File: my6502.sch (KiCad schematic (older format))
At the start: 64 parts, among them SW1 SW_MEC_5G, SW2 SW_MEC_5G, SW3 SW_Push_DPDT, SW4 SW_Push, SW5 SW_Push, SW6 SW_Push, SW7 SW_Push, SW8 SW_Push, SW9 SW_Push, U1 74HC00, U10 74HC00, U11 74HC00, U12 74HC00, U13 74HC00, U14 74HC00, U15 74HC00, U16 74HC00, U17 74HC00, U18 LM555xN, U2 LM555xN, U3 W65C02S, U4 LM555xN, U5 28C256, U6 65C22, U7 CY62256-70PC, U8 HD44780, U9 74HC00, X1 CXO_DIP14

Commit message: placed most components
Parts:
- removed U10, U11, U13, U14, U15, U16: 74HC00, Package_DIP:DIP-14_W7.62mm_LongPads, symbol 74xx:74HC00
- added C16, C17, C18: 100n, Capacitor_THT:C_Disc_D5.1mm_W3.2mm_P5.00mm, symbol Device:C
- added J1, J2, J3: Conn_01x08, Connector_PinHeader_2.54mm:PinHeader_1x08_P2.54mm_Vertical, symbol Connector_Generic:Conn_01x08
- added unit 2 of U12
- added unit 3 of U12
- added unit 4 of U12
- added unit 5 of U12
- added unit 2 of U17
- added unit 3 of U17
- added unit 4 of U17
- added unit 5 of U17
- added unit 2 of U9
- added unit 3 of U9
- added unit 4 of U9
- added unit 5 of U9
- D1, D2, D3: footprint LED_THT:LED_D5.0mm -> LED_THT:LED_D3.0mm
- JP1: footprint (none) -> Connector_PinHeader_2.54mm:PinHeader_1x03_P2.54mm_Vertical
- JP2, JP3, JP4: footprint (none) -> Connector_PinHeader_2.54mm:PinHeader_1x02_P2.54mm_Vertical
- SW1: value SW_MEC_5G -> Switch; footprint (none) -> Button_Switch_THT:SW_PUSH_6mm; symbol Switch:SW_MEC_5G -> Switch:SW_Push
- SW2: footprint (none) -> Button_Switch_THT:SW_PUSH_6mm; symbol Switch:SW_MEC_5G -> Switch:SW_Push
- SW4: footprint (none) -> Button_Switch_THT:SW_PUSH_6mm; PartID (none) -> Adafruit 4183
- SW5, SW6, SW7, SW8, SW9: footprint (none) -> Button_Switch_THT:SW_PUSH_6mm
- U8: footprint (none) -> Display:WC1602A
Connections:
- net +5V: now also C16.1, C17.1, C18.1, U12.14 (VCC), U9.14 (VCC)
- net A0: now also J1.1 (Pin_1)
- net A1: now also J1.2 (Pin_2)
- net A10: now also J3.3 (Pin_3)
- net A11: now also J3.4 (Pin_4)
- net A12: now also U1.13, J3.5 (Pin_5); no longer U1.2
- net A13: now also J3.6 (Pin_6)
- net A14: now also J3.7 (Pin_7)
- net A15: now also U1.1, U1.2, J3.8 (Pin_8); no longer U1.12, U1.13
- net A2: now also J1.3 (Pin_3)
- net A3: now also J1.4 (Pin_4)
- net A4: now also J1.5 (Pin_5)
- net A5: now also J1.6 (Pin_6)
- net A6: now also J1.7 (Pin_7)
- net A7: now also J1.8 (Pin_8)
- net A8: now also J3.1 (Pin_1)
- net A9: now also J3.2 (Pin_2)
- net CLK: now also U12.8
- net CLKSEL: now also U9.4, U9.5
- net D0: now also J2.1 (Pin_1)
- net D1: now also J2.2 (Pin_2)
- net D2: now also J2.3 (Pin_3)
- net D3: now also J2.4 (Pin_4)
- net D4: now also J2.5 (Pin_5)
- net D5: now also J2.6 (Pin_6)
- net D6: now also J2.7 (Pin_7)
- net D7: now also J2.8 (Pin_8)
- net GND: now also SW2.2, C16.2, C17.2, C18.2, U12.12, U12.13, U12.7 (GND), U17.10, U17.12, U17.13, U17.4, U17.5, U17.9, U9.7 (GND); no longer SW1.2 (A), SW2.3 (B), SW2.4 (B)
- net MCLK: now also U9.10
- net RESET: no longer SW2.2 (A)
- net ~A15: now also U1.3; no longer U1.11
- net at R3.2, U4.2 (TR): now also SW1.2; no longer SW1.3 (B), SW1.4 (B)
- net at U1.8: now also U1.12; no longer U1.1
- net at U17.2, U6.23 (CS2B): now also U1.11; no longer U1.3
- net at U9.3: now also U9.12
- net at JP1.1 (A): now also U9.11
- net at JP1.2 (C): now also U12.4
- net at U12.3: now also U12.5
- new net: U9.6, U9.9
- new net: U9.13, U9.8
- new net: U12.10, U12.6, U12.9
- no-connect marks 13 -> 16

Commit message: USB connector, overvoltage protection, ...
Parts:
- added D4: D_Zener, Diode_THT:D_A-405_P7.62mm_Horizontal, symbol Device:D_Zener
- added D5: LED, LED_THT:LED_D3.0mm, symbol Device:LED
- added J4: USB_B_Micro, Connector_USB:USB_Micro-B_Molex_47346-0001, symbol Connector:USB_B_Micro
- added R12: ? (low res), Resistor_THT:R_Axial_DIN0207_L6.3mm_D2.5mm_P7.62mm_Horizontal, symbol Device:R
- added R13: 220, Resistor_THT:R_Axial_DIN0207_L6.3mm_D2.5mm_P7.62mm_Horizontal, symbol Device:R
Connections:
- net +5V: now also D4.1 (K), D5.2 (A), R12.1
- net GND: now also D4.2 (A), J4.5 (GND), R13.1
- new net: D5.1 (K), R13.2
- new net USBVCC: J4.1 (VBUS), R12.2
- no-connect marks 16 -> 21
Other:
- note added: "TODO:\n- Mounting holes\n- Check if any more 6502 pins\n should be accessible (RDY? NMI?)\n- Validate all components! Not the least the USB conn.\n- Place all decoupler caps close to their IC's\n- Fancy silkscreen!\n- Is HLT connected anywhere?"
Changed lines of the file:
@@
 Text Label 12050 5600 0    50   ~ 0
 D7
-Wire Bus Line
-	9200 800  9200 2150
-Wire Bus Line
-	6900 800  6900 2150
-Wire Bus Line
-	7300 800  7300 2850
-Wire Bus Line
-	4900 800  4900 2850
-Wire Bus Line
-	14000 900  14000 2550
-Wire Bus Line
-	9650 900  9650 3550
-Wire Bus Line
-	4200 800  4200 4950
-Wire Bus Line
-	11700 800  11700 5500
 $Comp
 L Connector_Generic:Conn_01x08 J1
@@
 	1    0    0    -1
 $EndComp
+$Comp
+L Connector:USB_B_Micro J4
+U 1 1 60B35F2D
+P 10150 6900
+F 0 "J4" H 10207 7367 50  0000 C CNN
+F 1 "USB_B_Micro" H 10207 7276 50  0000 C CNN
+F 2 "Connector_USB:USB_Micro-B_Molex_47346-0001" H 10300 6850 50  0001 C CNN
+F 3 "~" H 10300 6850 50  0001 C CNN
+	1    10150 6900
+	1    0    0    -1
+$EndComp
+$Comp
+L power:GND #PWR0163
+U 1 1 60B392C5
+P 10150 7400
+F 0 "#PWR0163" H 10150 7150 50  0001 C CNN
+F 1 "GND" H 10155 7227 50  0000 C CNN
+F 2 "" H 10150 7400 50  0001 C CNN
+F 3 "" H 10150 7400 50  0001 C CNN
+	1    10150 7400
+	1    0    0    -1
+$EndComp
+Wire Wire Line
+	10150 7300 10150 7400
+Wire Wire Line
+	10450 6700 10800 6700
+Text Label 10500 6700 0    50   ~ 0
+USBVCC
+$Comp
+L Device:R R12
+U 1 1 60BB1CFB
+P 10950 6700
+F 0 "R12" H 11020 6746 50  0000 L CNN
+F 1 "? (low res)" H 11020 6655 50  0000 L CNN
+F 2 "Resistor_THT:R_Axial_DIN0207_L6.3mm_D2.5mm_P7.62mm_Horizontal" V 10880 6700 50  0001 C CNN
+F 3 "~" H 10950 6700 50  0001 C CNN
+	1    10950 6700
+	0    1    -1   0
+$EndComp
+$Comp
+L Device:D_Zener D4
+U 1 1 60BBC9CB
+P 11200 6950
+F 0 "D4" V 11154 7030 50  0000 L CNN
+F 1 "D_Zener" V 11245 7030 50  0000 L CNN
+F 2 "Diode_THT:D_A-405_P7.62mm_Horizontal" H 11200 6950 50  0001 C CNN
+F 3 "~" H 11200 6950 50  0001 C CNN
+	1    11200 6950
+	0    1    1    0
+$EndComp
+Wire Wire Line
+	11100 6700 11200 6700
+Wire Wire Line
+	11200 6700 11200 6800
+$Comp
+L power:GND #PWR0164
+U 1 1 60C904E5
+P 11200 7200
+F 0 "#PWR0164" H 11200 6950 50  0001 C CNN
+F 1 "GND" H 11205 7027 50  0000 C CNN
+F 2 "" H 11200 7200 50  0001 C CNN
+F 3 "" H 11200 7200 50  0001 C CNN
+	1    11200 7200
+	1    0    0    -1
+$EndComp
+Wire Wire Line
+	11200 7100 11200 7200
+$Comp
+L power:+5V #PWR0165
+U 1 1 60CCD1B2
+P 11200 6600
+F 0 "#PWR0165" H 11200 6450 50  0001 C CNN
+F 1 "+5V" H 11215 6773 50  0000 C CNN
+F 2 "" H 11200 6600 50  0001 C CNN
+F 3 "" H 11200 6600 50  0001 C CNN
+	1    11200 6600
+	-1   0    0    -1
+$EndComp
+Wire Wire Line
+	11200 6600 11200 6700
+Connection ~ 11200 6700
+NoConn ~ 10450 6900
+NoConn ~ 10450 7000
+NoConn ~ 10450 7100
+NoConn ~ 10050 7300
+NoConn ~ 12450 6250
+$Comp
+L Device:R R13
+U 1 1 60E322F4
+P 11700 7000
+F 0 "R13" H 11770 7046 50  0000 L CNN
+F 1 "220" H 11770 6955 50  0000 L CNN
+F 2 "Resistor_THT:R_Axial_DIN0207_L6.3mm_D2.5mm_P7.62mm_Horizontal" V 11630 7000 50  0001 C CNN
+F 3 "~" H 11700 7000 50  0001 C CNN
+	1    11700 7000
+	1    0    0    1
+$EndComp
+$Comp
+L Device:LED D5
+U 1 1 60E5E64D
+P 11500 6700
+F 0 "D5" H 11650 6650 50  0000 C CNN
+F 1 "LED" H 11500 6800 50  0000 C CNN
+F 2 "LED_THT:LED_D3.0mm" H 11500 6700 50  0001 C CNN
+F 3 "~" H 11500 6700 50  0001 C CNN
+	1    11500 6700
+	-1   0    0    1
+$EndComp
+Wire Wire Line
+	11200 6700 11350 6700
+Wire Wire Line
+	11650 6700 11700 6700
+Wire Wire Line
+	11700 6700 11700 6850
+$Comp
+L power:GND #PWR0166
+U 1 1 60F053B9
+P 11700 7200
+F 0 "#PWR0166" H 11700 6950 50  0001 C CNN
+F 1 "GND" H 11705 7027 50  0000 C CNN
+F 2 "" H 11700 7200 50  0001 C CNN
+F 3 "" H 11700 7200 50  0001 C CNN
+	1    11700 7200
+	1    0    0    -1
+$EndComp
+Wire Wire Line
+	11700 7150 11700 7200
+Wire Bus Line
+	9200 800  9200 2150
+Wire Bus Line
+	6900 800  6900 2150
+Wire Bus Line
+	7300 800  7300 2850
+Wire Bus Line
+	4900 800  4900 2850
+Wire Bus Line
+	14000 900  14000 2550
+Wire Bus Line
+	9650 900  9650 3550
+Wire Bus Line
+	4200 800  4200 4950
+Wire Bus Line
+	11700 800  11700 5500
+Text Notes -2500 600  0    50   ~ 0
+TODO:\n- Mounting holes\n- Check if any more 6502 pins\n    should be accessible (RDY? NMI?)\n- Validate all components! Not the least the USB conn.\n- Place all decoupler caps close to their IC's\n- Fancy silkscreen!\n- Is HLT connected anywhere?
 $EndSCHEMATC

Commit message: Mostly minor adjustments
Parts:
- RV2, RV3: footprint Resistor_THT:R_Axial_DIN0207_L6.3mm_D2.5mm_P7.62mm_Horizontal -> Potentiometer_THT:Potentiometer_Piher_PT-6-V_Vertical
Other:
- moved on the sheet: C1, U1E
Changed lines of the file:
@@
 L 74xx:74HC00 U1
 U 5 1 6018728D
-P 12150 8950
-F 0 "U1" H 12380 8996 50  0000 L CNN
-F 1 "74HC00" H 12380 8905 50  0000 L CNN
-F 2 "Package_DIP:DIP-14_W7.62mm_LongPads" H 12150 8950 50  0001 C CNN
-F 3 "http://www.ti.com/lit/gpn/sn74hc00" H 12150 8950 50  0001 C CNN
-	5    12150 8950
+P 11900 8950
+F 0 "U1" H 12130 8996 50  0000 L CNN
+F 1 "74HC00" H 12130 8905 50  0000 L CNN
+F 2 "Package_DIP:DIP-14_W7.62mm_LongPads" H 11900 8950 50  0001 C CNN
+F 3 "http://www.ti.com/lit/gpn/sn74hc00" H 11900 8950 50  0001 C CNN
+	5    11900 8950
 	1    0    0    -1
 $EndComp
@@
 L Device:C C1
 U 1 1 6018D610
-P 11800 8950
-F 0 "C1" H 11650 9050 50  0000 L CNN
-F 1 "100n" V 11750 8700 50  0000 L CNN
-F 2 "Capacitor_THT:C_Disc_D5.1mm_W3.2mm_P5.00mm" H 11838 8800 50  0001 C CNN
-F 3 "~" H 11800 8950 50  0001 C CNN
-	1    11800 8950
+P 11500 8900
+F 0 "C1" H 11350 9000 50  0000 L CNN
+F 1 "100n" V 11450 8650 50  0000 L CNN
+F 2 "Capacitor_THT:C_Disc_D5.1mm_W3.2mm_P5.00mm" H 11538 8750 50  0001 C CNN
+F 3 "~" H 11500 8900 50  0001 C CNN
+	1    11500 8900
 	1    0    0    -1
 $EndComp
 Wire Wire Line
-	11800 8800 11800 8450
+	11500 8450 11900 8450
 Wire Wire Line
-	11800 8450 12150 8450
+	11500 9050 11500 9450
 Wire Wire Line
-	11800 9100 11800 9450
-Wire Wire Line
-	11800 9450 12150 9450
-$Comp
-L power:+5V #PWR0113
-U 1 1 601B7EDC
-P 12150 8400
-F 0 "#PWR0113" H 12150 8250 50  0001 C CNN
-F 1 "+5V" H 12165 8573 50  0000 C CNN
-F 2 "" H 12150 8400 50  0001 C CNN
-F 3 "" H 12150 8400 50  0001 C CNN
-	1    12150 8400
-	1    0    0    -1
-$EndComp
-Wire Wire Line
-	12150 8400 12150 8450
-$Comp
-L power:GND #PWR0114
-U 1 1 601BA2BC
-P 12150 9500
-F 0 "#PWR0114" H 12150 9250 50  0001 C CNN
-F 1 "GND" H 12155 9327 50  0000 C CNN
-F 2 "" H 12150 9500 50  0001 C CNN
-F 3 "" H 12150 9500 50  0001 C CNN
-	1    12150 9500
-	1    0    0    -1
-$EndComp
-Wire Wire Line
-	12150 9500 12150 9450
-Connection ~ 12150 9450
+	11500 9450 11900 9450
 $Comp
 L power:+5V #PWR0115
@@
 	1    0    0    -1
 $EndComp
-Connection ~ 12150 8450
 Wire Wire Line
 	2800 7200 2800 7250
@@
 Astable oscillator
 Wire Notes Line
-	11450 9800 11450 7800
+	8700 9800 8700 7800
 Wire Notes Line
-	11450 7800 15900 7800
+	8700 7800 15900 7800
 Wire Notes Line
 	15900 7800 15900 9800
 Wire Notes Line
-	15900 9800 11450 9800
+	15900 9800 8700 9800
 Text Notes 11550 8050 0    98   ~ 0
 Decoupling Capacitors
@@
 F 0 "RV2" H 12000 1600 50  0000 R CNN
 F 1 "10k?" H 12000 1500 50  0000 R CNN
-F 2 "Resistor_THT:R_Axial_DIN0207_L6.3mm_D2.5mm_P7.62mm_Horizontal" H 12100 1550 50  0001 C CNN
+F 2 "Potentiometer_THT:Potentiometer_Piher_PT-6-V_Vertical" H 12100 1550 50  0001 C CNN
 F 3 "~" H 12100 1550 50  0001 C CNN
 	1    12100 1550
@@
 F 0 "RV3" H 12150 2050 50  0000 R CNN
 F 1 "10k?" H 12150 1950 50  0000 R CNN
-F 2 "Resistor_THT:R_Axial_DIN0207_L6.3mm_D2.5mm_P7.62mm_Horizontal" H 12250 2000 50  0001 C CNN
+F 2 "Potentiometer_THT:Potentiometer_Piher_PT-6-V_Vertical" H 12250 2000 50  0001 C CNN
 F 3 "~" H 12250 2000 50  0001 C CNN
 	1    12250 2000
@@
 U 5 1 60C17C42
 P 11050 8950
-F 0 "U9" H 11050 9275 50  0000 C CNN
-F 1 "74HC00" H 11050 9184 50  0000 C CNN
+F 0 "U9" H 11150 9300 50  0000 C CNN
+F 1 "74HC00" H 11050 8950 50  0000 C CNN
 F 2 "Package_DIP:DIP-14_W7.62mm_LongPads" H 11050 8950 50  0001 C CNN
 F 3 "http://www.ti.com/lit/gpn/sn74hc00" H 11050 8950 50  0001 C CNN
@@
 U 5 1 60C78F3C
 P 10150 8950
-F 0 "U12" H 10150 9275 50  0000 C CNN
-F 1 "74HC00" H 10150 9184 50  0000 C CNN
+F 0 "U12" H 10300 9300 50  0000 C CNN
+F 1 "74HC00" H 10150 8950 50  0000 C CNN
 F 2 "Package_DIP:DIP-14_W7.62mm_LongPads" H 10150 8950 50  0001 C CNN
 F 3 "http://www.ti.com/lit/gpn/sn74hc00" H 10150 8950 50  0001 C CNN
@@
 U 5 1 60E661A5
 P 9450 8950
-F 0 "U17" H 9650 9100 50  0000 C CNN
-F 1 "74HC00" H 9700 8800 50  0000 C CNN
+F 0 "U17" H 9600 9300 50  0000 C CNN
+F 1 "74HC00" H 9450 8950 50  0000 C CNN
 F 2 "Package_DIP:DIP-14_W7.62mm_LongPads" H 9450 8950 50  0001 C CNN
 F 3 "http://www.ti.com/lit/gpn/sn74hc00" H 9450 8950 50  0001 C CNN
@@
 Wire Wire Line
 	11700 7150 11700 7200
+Text Notes -2500 600  0    50   ~ 0
+TODO:\n- Mounting holes\n- Check if any more 6502 pins\n    should be accessible (RDY? NMI?)\n- Validate all components! Not the least the USB conn.\n- Place all decoupler caps close to their IC's\n- Fancy silkscreen!\n- Is HLT connected anywhere?
+Wire Wire Line
+	11500 8750 11500 8450
+Wire Wire Line
+	11050 8450 11500 8450
+Connection ~ 11050 8450
+Connection ~ 11500 8450
+Wire Wire Line
+	11050 9450 11500 9450
+Connection ~ 11050 9450
+Connection ~ 11500 9450
 Wire Bus Line
-	9200 800  9200 2150
+	9650 900  9650 3550
 Wire Bus Line
-	6900 800  6900 2150
+	9200 800  9200 2150
 Wire Bus Line
-	7300 800  7300 2850
+	14000 900  14000 2550
 Wire Bus Line
 	4900 800  4900 2850
 Wire Bus Line
-	14000 900  14000 2550
-Wire Bus Line
-	9650 900  9650 3550
+	6900 800  6900 2150
 Wire Bus Line
 	4200 800  4200 4950
 Wire Bus Line
 	11700 800  11700 5500
-Text Notes -2500 600  0    50   ~ 0
-TODO:\n- Mounting holes\n- Check if any more 6502 pins\n    should be accessible (RDY? NMI?)\n- Validate all components! Not the least the USB conn.\n- Place all decoupler caps close to their IC's\n- Fancy silkscreen!\n- Is HLT connected anywhere?
+Wire Bus Line
+	7300 800  7300 2850
 $EndSCHEMATC

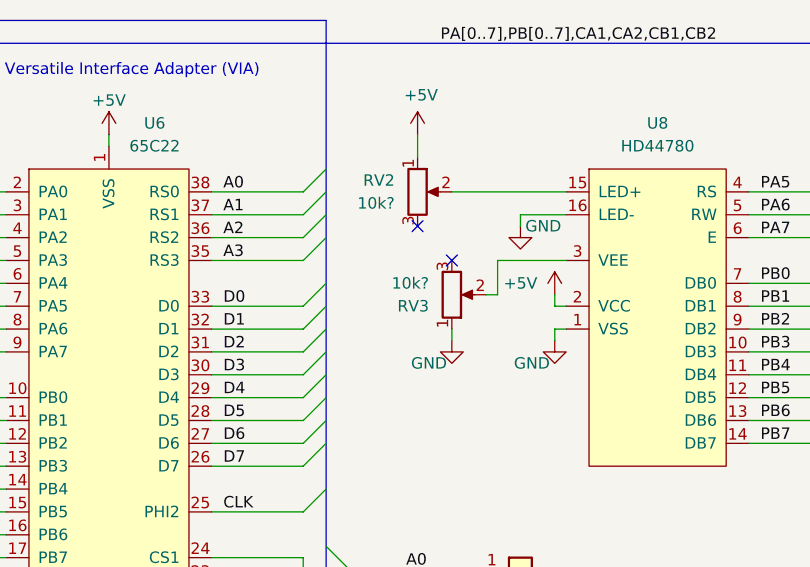
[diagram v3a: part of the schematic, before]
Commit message: Some components decided on and initial routing
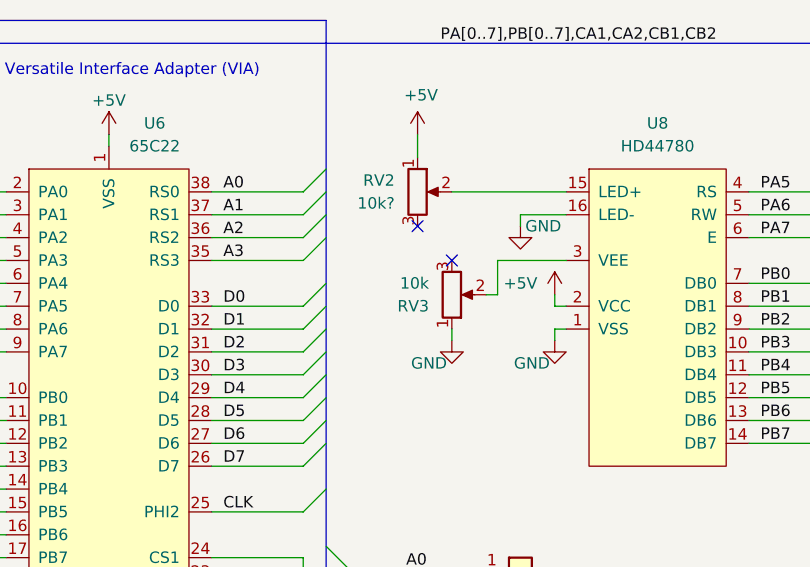
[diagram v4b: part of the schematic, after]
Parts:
- RV1: footprint Resistor_THT:R_Axial_DIN0207_L6.3mm_D2.5mm_P7.62mm_Horizontal -> Potentiometer_THT:Potentiometer_Bourns_3386F_Vertical; Digi-Key (none) -> 3386X-1-105TLF-ND; MFN (none) -> Bourns; MFP (none) -> 3386F-1-105TLF; Mouser (none) -> 652-3386F-1-105TLF
- RV2: footprint Potentiometer_THT:Potentiometer_Piher_PT-6-V_Vertical -> Potentiometer_THT:Potentiometer_Bourns_3296W_Vertical
- RV3: value 10k? -> 10k; footprint Potentiometer_THT:Potentiometer_Piher_PT-6-V_Vertical -> Potentiometer_THT:Potentiometer_Bourns_3296W_Vertical
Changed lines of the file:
@@
 F 0 "RV1" H 3100 8250 50  0000 R CNN
 F 1 "1M" H 3100 8100 50  0000 R CNN
-F 2 "Resistor_THT:R_Axial_DIN0207_L6.3mm_D2.5mm_P7.62mm_Horizontal" H 2800 8150 50  0001 C CNN
+F 2 "Potentiometer_THT:Potentiometer_Bourns_3386F_Vertical" H 2800 8150 50  0001 C CNN
 F 3 "~" H 2800 8150 50  0001 C CNN
+F 4 "Bourns" H 2800 8150 50  0001 C CNN "MFN"
+F 5 "3386F-1-105TLF" H 2800 8150 50  0001 C CNN "MFP"
+F 6 "3386X-1-105TLF-ND" H 2800 8150 50  0001 C CNN "Digi-Key"
+F 7 " 652-3386F-1-105TLF " H 2800 8150 50  0001 C CNN "Mouser"
 	1    2800 8150
 	1    0    0    -1
@@
 F 0 "RV2" H 12000 1600 50  0000 R CNN
 F 1 "10k?" H 12000 1500 50  0000 R CNN
-F 2 "Potentiometer_THT:Potentiometer_Piher_PT-6-V_Vertical" H 12100 1550 50  0001 C CNN
+F 2 "Potentiometer_THT:Potentiometer_Bourns_3296W_Vertical" H 12100 1550 50  0001 C CNN
 F 3 "~" H 12100 1550 50  0001 C CNN
 	1    12100 1550
@@
 P 12250 2000
 F 0 "RV3" H 12150 2050 50  0000 R CNN
-F 1 "10k?" H 12150 1950 50  0000 R CNN
-F 2 "Potentiometer_THT:Potentiometer_Piher_PT-6-V_Vertical" H 12250 2000 50  0001 C CNN
+F 1 "10k" H 12150 1950 50  0000 R CNN
+F 2 "Potentiometer_THT:Potentiometer_Bourns_3296W_Vertical" H 12250 2000 50  0001 C CNN
 F 3 "~" H 12250 2000 50  0001 C CNN
 	1    12250 2000
@@
 Connection ~ 11500 9450
 Wire Bus Line
-	9650 900  9650 3550
+	9200 800  9200 2150
 Wire Bus Line
-	9200 800  9200 2150
+	6900 800  6900 2150
+Wire Bus Line
+	7300 800  7300 2850
+Wire Bus Line
+	4900 800  4900 2850
 Wire Bus Line
 	14000 900  14000 2550
 Wire Bus Line
-	4900 800  4900 2850
-Wire Bus Line
-	6900 800  6900 2150
+	9650 900  9650 3550
 Wire Bus Line
 	4200 800  4200 4950
 Wire Bus Line
 	11700 800  11700 5500
-Wire Bus Line
-	7300 800  7300 2850
 $EndSCHEMATC

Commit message: many routes
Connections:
- net +5V: now also U17.14 (VCC)
- net GND: now also U17.7 (GND)
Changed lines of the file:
@@
 	14350 6450 14400 6450
 Wire Wire Line
-	9100 8450 9800 8450
-Wire Wire Line
-	9100 9450 9800 9450
+	9100 8450 9450 8450
+Wire Wire Line
+	9100 9450 9450 9450
 Wire Wire Line
 	14350 6450 14350 6250
@@
 Wire Bus Line
 	11700 800  11700 5500
+Connection ~ 9450 8450
+Wire Wire Line
+	9450 8450 9800 8450
+Connection ~ 9450 9450
+Wire Wire Line
+	9450 9450 9800 9450
 $EndSCHEMATC
